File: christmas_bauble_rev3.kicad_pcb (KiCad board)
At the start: 2 copper layers, 80 x 80 mm, 32 parts, among them SW1 SWITCH_INV, SW2 SW_PUSH, SW3 SW_PUSH, U1 LOGIC_SMD_XOR, U2 595_SHIFT, U3 555

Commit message: Some minor changes. This is the version that went into production. Woop woop \o/
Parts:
- moved SYM 3.13 mm to (120.4, 61.8)
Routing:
- net Net-(D2-Pad2): track 14.7 -> 17.1 mm
- net GND: track 419.8 -> 418.4 mm
- net Net-(D4-Pad2): track 10.0 -> 10.8 mm
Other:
- net class DirtyPCB added: clearance 0.0127, trace_width 0.0127, via_dia 0.6, via_drill 0.4
- rule trace_min: 0.2 -> 0.0127
- board text added: "Kookies Christmas Bauble Revision 3.1 13-11-2015"
- board text removed: "Kookies Christmas Bauble Revision 3.0 13-09-2015"

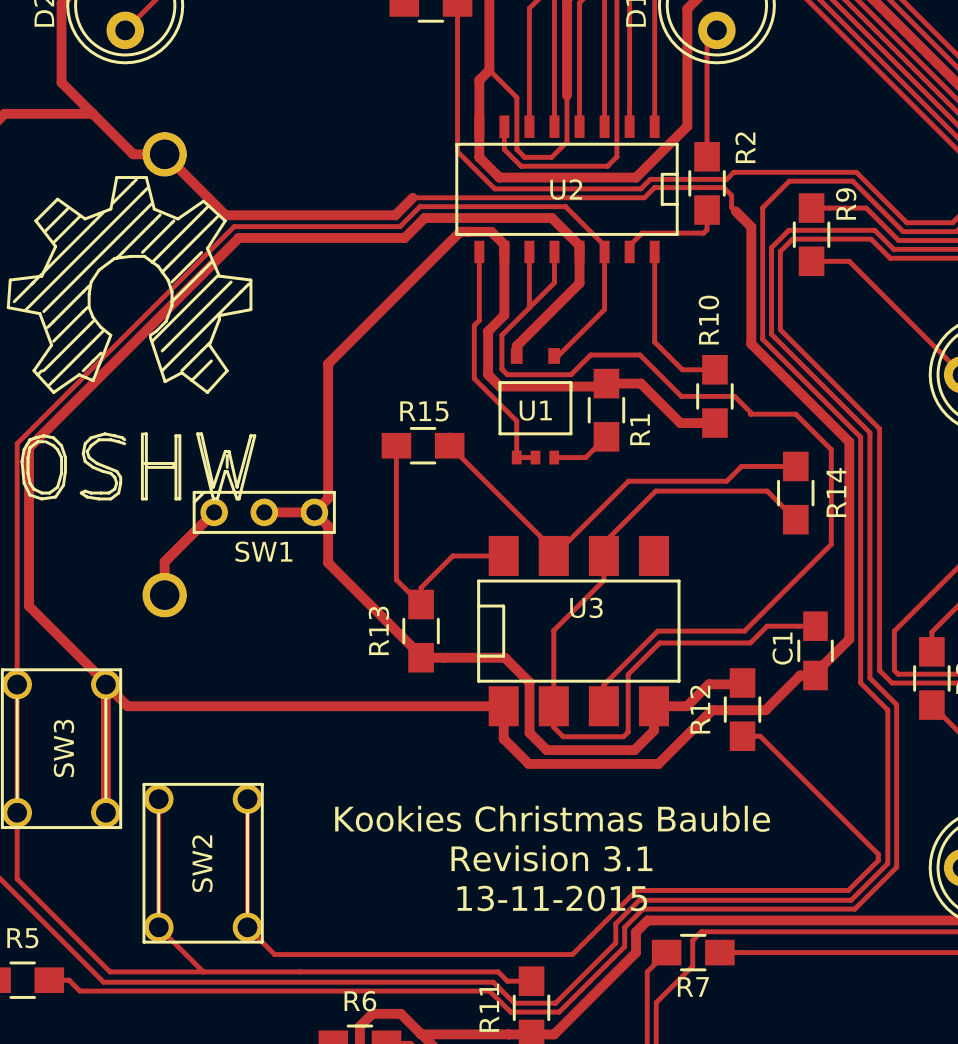
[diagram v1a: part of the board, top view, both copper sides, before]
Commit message: Changing batteries on the board to 2 20mm coin cell batteries in paralell for longer lifetime. Routing batteries on the back via SMD holders.
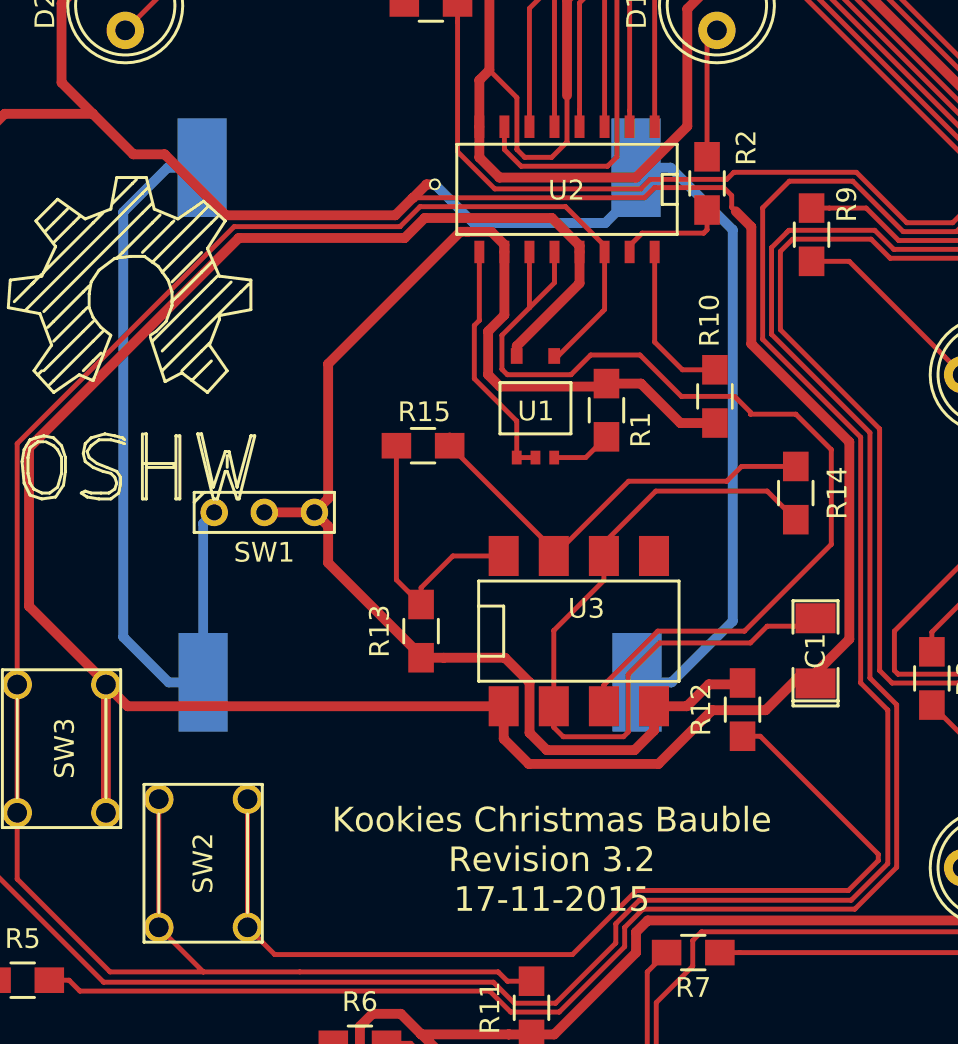
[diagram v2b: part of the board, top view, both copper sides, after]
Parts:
- added BT2: Battery, kookie_utilities:20mm_coin_bat_smd, B.Cu at (134.9, 74.5)
- BT1: footprint kookie_utilities:COIN_BAT_HOLDER -> kookie_utilities:20mm_coin_bat_smd
- C1: footprint Capacitors_SMD:C_0805_HandSoldering -> SMD_Packages:SMD-1206_Pol
- moved BT1 20.3 mm to (134.9, 100.6), turned to 0 degrees
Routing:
- net GND: track 418.4 -> 464.9 mm, vias 0 -> 1
- net Net-(BT1-Pad1): track 8.78 -> 41.6 mm
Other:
- board text added: "Kookies Christmas Bauble Revision 3.2 17-11-2015"
- board text removed: "Kookies Christmas Bauble Revision 3.1 13-11-2015"
